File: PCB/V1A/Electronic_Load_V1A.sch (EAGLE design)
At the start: 139 parts, among them IC201 OPA77P, IC202 OPA77P, IC203 OPA77P, IC204 OPA77P, IC205 OPA77P, IC301 MAX743CPE, IC302 7805T, IC303 7805T, IC304 7905, J101 +, J102 -, J103 +, J104 -, Q101 SIRC10DP, Q102 SIRC10DP, Q103 SIRC10DP, Q104 IXTK102N65X2PADUP-, Q105 SIRC10DP, Q106 SIRC10DP, Q107 SIRC10DP, Q108 IXTK102N65X2PADUP, U201 LTC1865-MSOP, U202 LTC1865-MSOP, U203 LTC1865-MSOP, U401 AD420, U402 AD420, U403 LT1014

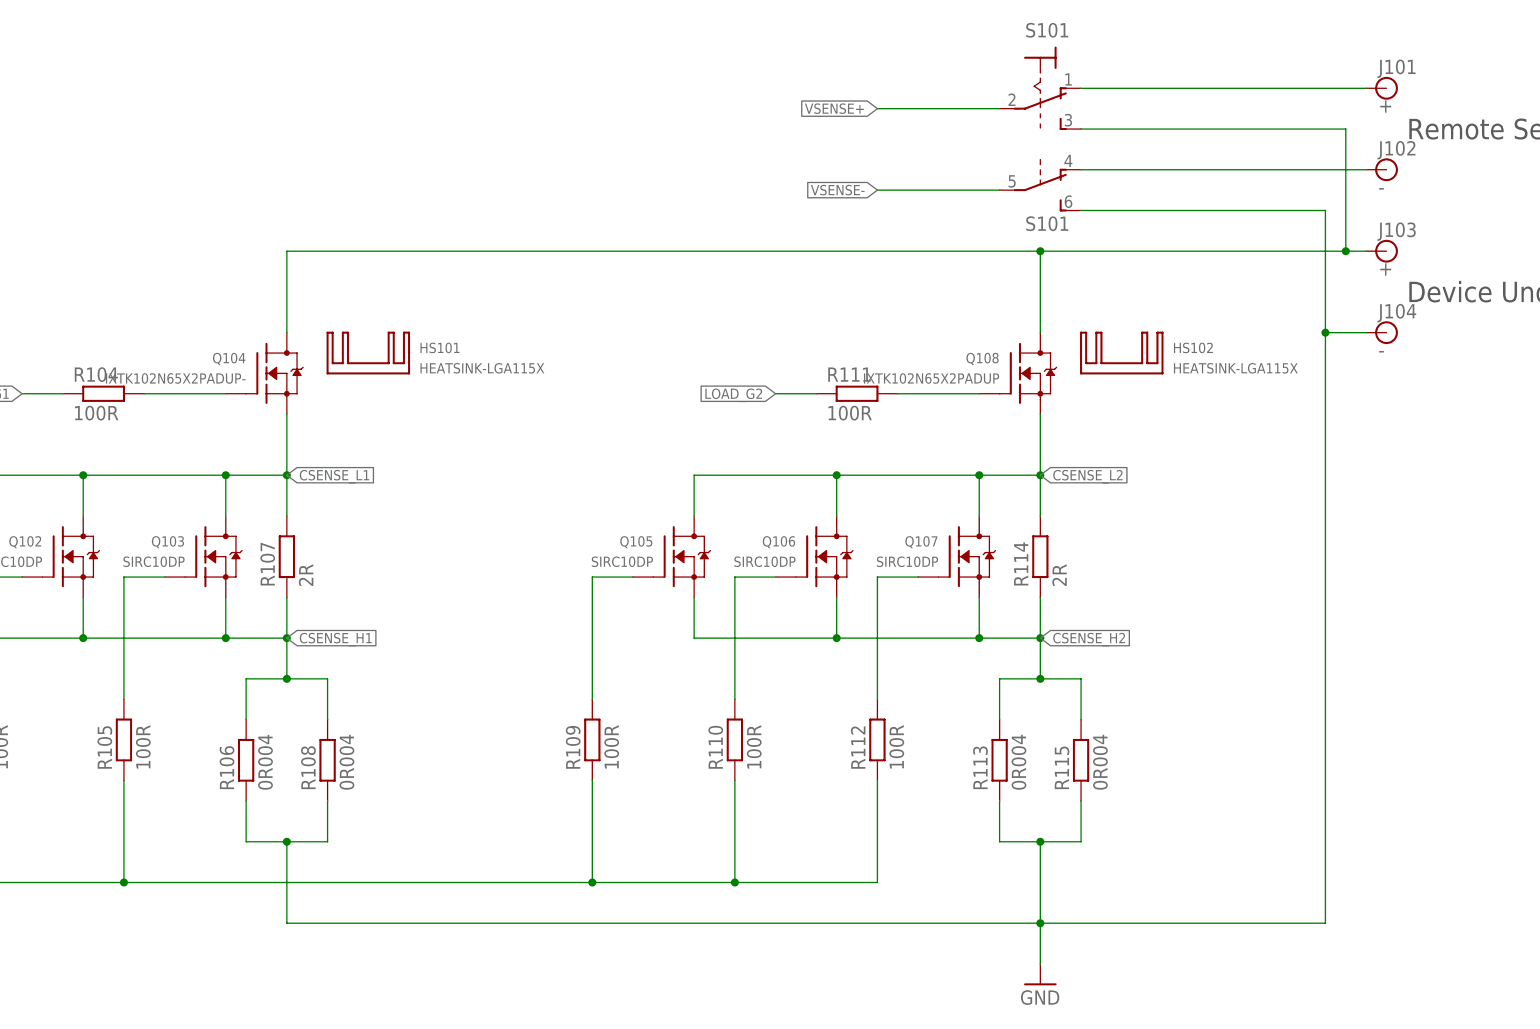
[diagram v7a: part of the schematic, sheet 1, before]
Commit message: Board layout work
PCB is 100x100mm 2 layer 2oz. MOSFETs mounted between a plate and heatsinks, control board mounted under the plate. DUT+ connected directly from binding post to drains, gates and sources connected to PCB with wires.
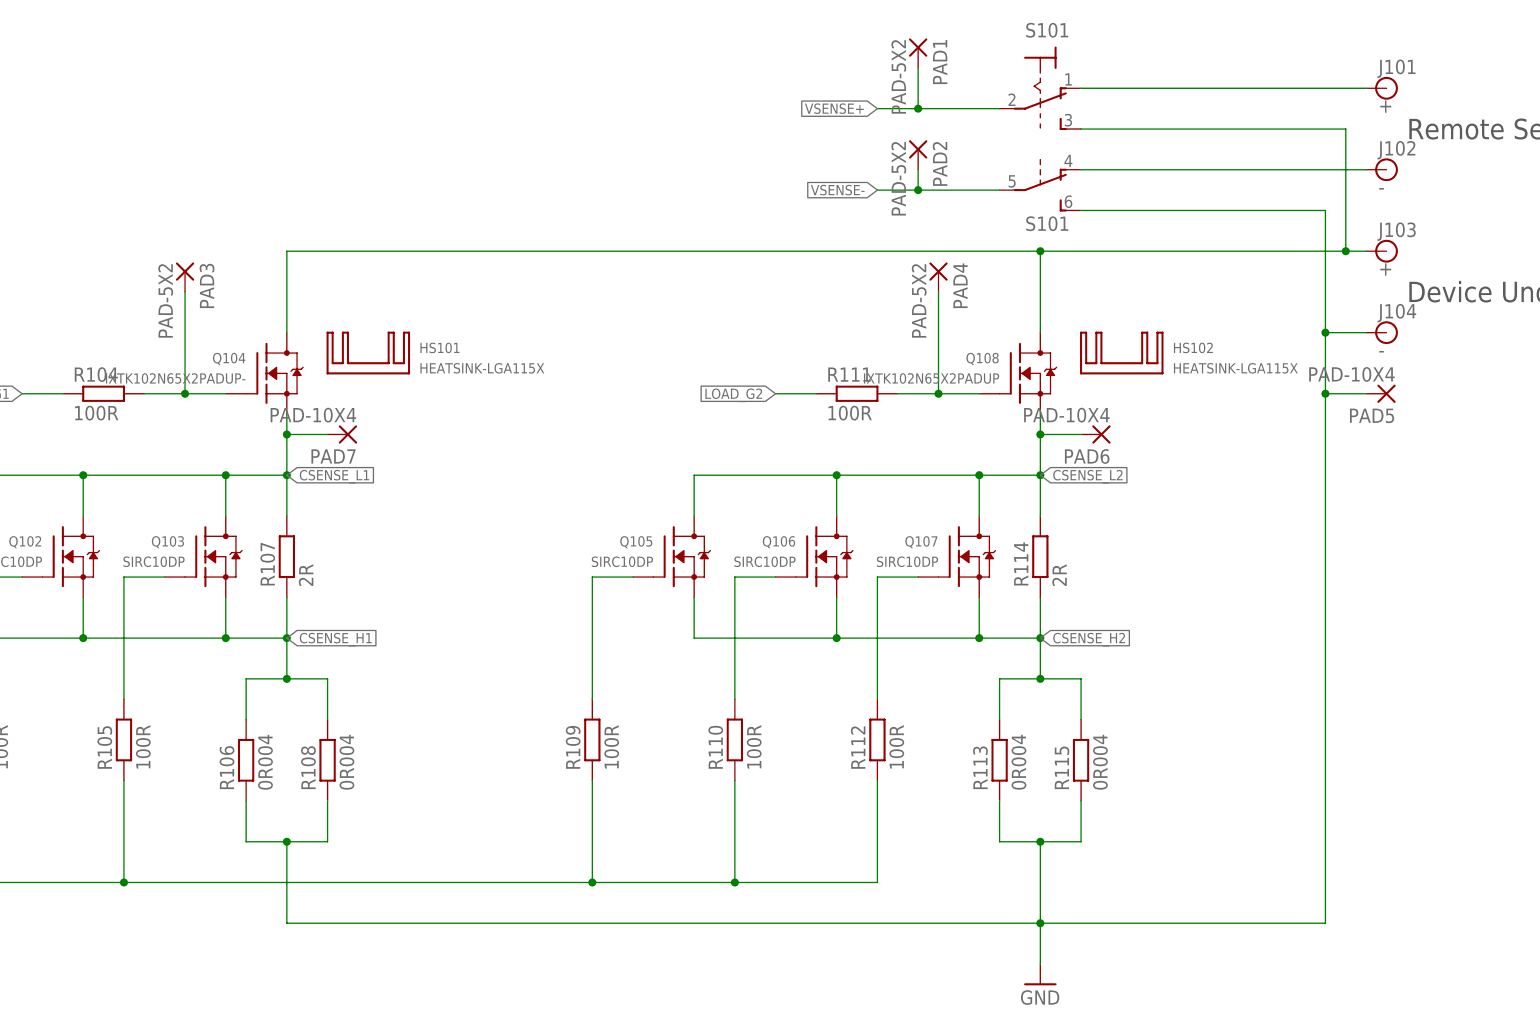
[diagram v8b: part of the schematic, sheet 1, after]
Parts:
- added PAD1, PAD2, PAD3, PAD4: PAD-5X2, pads:PAD-5X2
- added PAD5, PAD6, PAD7: PAD-10X4, pads:PAD-10X4
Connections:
- net CSENSE_L1: now also PAD7.P
- net CSENSE_L2: now also PAD6.P
- net GND: now also PAD5.P
- net N$52: now also PAD3.P
- net N$54: now also PAD4.P
- net VSENSE+: now also PAD1.P
- net VSENSE-: now also PAD2.P
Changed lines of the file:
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@@
 <?xml version="1.0" encoding="utf-8"?>
 <!DOCTYPE eagle SYSTEM "eagle.dtd">
-<eagle version="9.0.1">
+<eagle version="9.0.0">
 <drawing>
 <settings>
@@
 </variantdefs>
 <classes>
-<class number="0" name="default" width="0.2032" drill="0">
+<class number="0" name="default" width="0.1524" drill="0">
 <clearance class="0" value="0.2032"/>
 </class>
-<class number="1" name="HV" width="0.2032" drill="0">
-<clearance class="1" value="3.85"/>
+<class number="1" name="500V" width="0.1524" drill="0">
+<clearance class="1" value="3.5"/>
+</class>
+<class number="2" name="50V" width="0" drill="0">
+<clearance class="2" value="0.6"/>
 </class>
 </classes>
@@
 <part name="GND212" library="supply1" library_urn="urn:adsk.eagle:library:371" deviceset="GND" device=""/>
 <part name="P-205" library="supply1" library_urn="urn:adsk.eagle:library:371" deviceset="-15V" device=""/>
+<part name="PAD3" library="pads" deviceset="PAD" device="-5X2"/>
+<part name="PAD4" library="pads" deviceset="PAD" device="-5X2"/>
+<part name="PAD1" library="pads" deviceset="PAD" device="-5X2"/>
+<part name="PAD2" library="pads" deviceset="PAD" device="-5X2"/>
+<part name="PAD5" library="pads" deviceset="PAD" device="-10X4"/>
+<part name="PAD6" library="pads" deviceset="PAD" device="-10X4"/>
+<part name="PAD7" library="pads" deviceset="PAD" device="-10X4"/>
 </parts>
 <sheets>
@@
 <instance part="R108" gate="G$1" x="99.06" y="86.36" rot="R90"/>
 <instance part="R115" gate="G$1" x="193.04" y="86.36" rot="R90"/>
+<instance part="PAD3" gate="G$1" x="81.28" y="147.32" rot="R270"/>
+<instance part="PAD4" gate="G$1" x="175.26" y="147.32" rot="R270"/>
+<instance part="PAD1" gate="G$1" x="172.72" y="175.26" rot="R270"/>
+<instance part="PAD2" gate="G$1" x="172.72" y="162.56" rot="R270"/>
+<instance part="PAD5" gate="G$1" x="231.14" y="132.08" rot="R180"/>
+<instance part="PAD6" gate="G$1" x="195.58" y="127" rot="R180"/>
+<instance part="PAD7" gate="G$1" x="101.6" y="127" rot="R180"/>
 </instances>
 <busses>
@@
 <wire x1="223.52" y1="154.94" x2="223.52" y2="139.7" width="0.1524" layer="91"/>
 <junction x="223.52" y="139.7"/>
-<wire x1="223.52" y1="139.7" x2="223.52" y2="66.04" width="0.1524" layer="91"/>
+<wire x1="223.52" y1="139.7" x2="223.52" y2="132.08" width="0.1524" layer="91"/>
+<wire x1="223.52" y1="132.08" x2="223.52" y2="66.04" width="0.1524" layer="91"/>
 <wire x1="223.52" y1="66.04" x2="187.96" y2="66.04" width="0.1524" layer="91"/>
 <pinref part="R108" gate="G$1" pin="1"/>
@@
 <wire x1="187.96" y1="76.2" x2="187.96" y2="66.04" width="0.1524" layer="91"/>
 <junction x="187.96" y="76.2"/>
+<pinref part="PAD5" gate="G$1" pin="P"/>
+<wire x1="228.6" y1="132.08" x2="223.52" y2="132.08" width="0.1524" layer="91"/>
+<junction x="223.52" y="132.08"/>
 </segment>
 </net>
 <net name="N$52" class="0">
 <segment>
-<wire x1="76.2" y1="132.08" x2="86.36" y2="132.08" width="0.1524" layer="91"/>
+<wire x1="76.2" y1="132.08" x2="81.28" y2="132.08" width="0.1524" layer="91"/>
 <pinref part="R104" gate="G$1" pin="2"/>
 <pinref part="Q104" gate="G$1" pin="G"/>
+<pinref part="PAD3" gate="G$1" pin="P"/>
+<wire x1="81.28" y1="132.08" x2="86.36" y2="132.08" width="0.1524" layer="91"/>
+<wire x1="81.28" y1="144.78" x2="81.28" y2="132.08" width="0.1524" layer="91"/>
+<junction x="81.28" y="132.08"/>
 </segment>
 </net>
@@
 <segment>
 <pinref part="S101" gate="B" pin="P"/>
-<wire x1="182.88" y1="157.48" x2="167.64" y2="157.48" width="0.1524" layer="91"/>
+<wire x1="182.88" y1="157.48" x2="172.72" y2="157.48" width="0.1524" layer="91"/>
 <label x="167.64" y="157.48" size="1.27" layer="95" font="vector" ratio="12" rot="R180" xref="yes"/>
-</segment>
-</net>
-<net name="VSENSE+" class="0">
+<wire x1="172.72" y1="157.48" x2="167.64" y2="157.48" width="0.1524" layer="91"/>
+<wire x1="172.72" y1="160.02" x2="172.72" y2="157.48" width="0.1524" layer="91"/>
+<junction x="172.72" y="157.48"/>
+<pinref part="PAD2" gate="G$1" pin="P"/>
+</segment>
+</net>
+<net name="VSENSE+" class="1">
 <segment>
 <pinref part="S101" gate="1" pin="P"/>
-<wire x1="182.88" y1="167.64" x2="167.64" y2="167.64" width="0.1524" layer="91"/>
+<wire x1="182.88" y1="167.64" x2="172.72" y2="167.64" width="0.1524" layer="91"/>
 <label x="167.64" y="167.64" size="1.27" layer="95" font="vector" ratio="12" rot="R180" xref="yes"/>
+<wire x1="172.72" y1="167.64" x2="167.64" y2="167.64" width="0.1524" layer="91"/>
+<wire x1="172.72" y1="172.72" x2="172.72" y2="167.64" width="0.1524" layer="91"/>
+<junction x="172.72" y="167.64"/>
+<pinref part="PAD1" gate="G$1" pin="P"/>
 </segment>
 </net>
@@
 <segment>
 <pinref part="R111" gate="G$1" pin="2"/>
-<wire x1="170.18" y1="132.08" x2="180.34" y2="132.08" width="0.1524" layer="91"/>
+<wire x1="170.18" y1="132.08" x2="175.26" y2="132.08" width="0.1524" layer="91"/>
 <pinref part="Q108" gate="G$1" pin="G"/>
+<pinref part="PAD4" gate="G$1" pin="P"/>
+<wire x1="175.26" y1="132.08" x2="180.34" y2="132.08" width="0.1524" layer="91"/>
+<wire x1="175.26" y1="144.78" x2="175.26" y2="132.08" width="0.1524" layer="91"/>
+<junction x="175.26" y="132.08"/>
 </segment>
 </net>
@@
 <label x="93.98" y="121.92" size="1.27" layer="95" font="vector" ratio="12" xref="yes"/>
 <pinref part="Q104" gate="G$1" pin="S"/>
-<wire x1="93.98" y1="129.54" x2="93.98" y2="121.92" width="0.1524" layer="91"/>
+<wire x1="93.98" y1="129.54" x2="93.98" y2="127" width="0.1524" layer="91"/>
 <junction x="93.98" y="121.92"/>
 <pinref part="Q102" gate="G$1" pin="D"/>
+<wire x1="93.98" y1="127" x2="93.98" y2="121.92" width="0.1524" layer="91"/>
 <wire x1="68.58" y1="116.84" x2="68.58" y2="121.92" width="0.1524" layer="91"/>
 <pinref part="Q101" gate="G$1" pin="D"/>
@@
 <wire x1="86.36" y1="116.84" x2="86.36" y2="121.92" width="0.1524" layer="91"/>
 <junction x="86.36" y="121.92"/>
+<pinref part="PAD7" gate="G$1" pin="P"/>
+<wire x1="99.06" y1="127" x2="93.98" y2="127" width="0.1524" layer="91"/>
+<junction x="93.98" y="127"/>
 </segment>
 </net>
@@
 <label x="187.96" y="121.92" size="1.27" layer="95" font="vector" ratio="12" xref="yes"/>
 <pinref part="Q108" gate="G$1" pin="S"/>
-<wire x1="187.96" y1="129.54" x2="187.96" y2="121.92" width="0.1524" layer="91"/>
+<wire x1="187.96" y1="129.54" x2="187.96" y2="127" width="0.1524" layer="91"/>
 <junction x="187.96" y="121.92"/>
 <pinref part="Q107" gate="G$1" pin="D"/>
+<wire x1="187.96" y1="127" x2="187.96" y2="121.92" width="0.1524" layer="91"/>
 <wire x1="180.34" y1="116.84" x2="180.34" y2="121.92" width="0.1524" layer="91"/>
 <junction x="180.34" y="121.92"/>
@@
 <wire x1="144.78" y1="121.92" x2="162.56" y2="121.92" width="0.1524" layer="91"/>
 <junction x="162.56" y="121.92"/>
+<pinref part="PAD6" gate="G$1" pin="P"/>
+<wire x1="193.04" y1="127" x2="187.96" y2="127" width="0.1524" layer="91"/>
+<junction x="187.96" y="127"/>
 </segment>
 </net>
@@
 </segment>
 </net>
-<net name="N$73" class="0">
+<net name="N$73" class="2">
 <segment>
 <pinref part="R216" gate="G$1" pin="2"/>
@@
 </segment>
 </net>
-<net name="N$78" class="0">
+<net name="N$78" class="2">
 <segment>
 <pinref part="R211" gate="G$1" pin="1"/>
@@
 </segment>
 </net>
-<net name="N$79" class="0">
+<net name="N$79" class="2">
 <segment>
 <pinref part="R212" gate="G$1" pin="1"/>
@@
 </segment>
 </net>
-<net name="N$84" class="0">
+<net name="N$84" class="2">
 <segment>
 <pinref part="R213" gate="G$1" pin="1"/>
@@
 </segment>
 </net>
-<net name="N$85" class="0">
+<net name="N$85" class="2">
 <segment>
 <pinref part="R210" gate="G$1" pin="2"/>
@@
 </segment>
 </net>
-<net name="N$86" class="0">
+<net name="N$86" class="2">
 <segment>
 <pinref part="R209" gate="G$1" pin="2"/>
@@
 </segment>
 </net>
-<net name="N$87" class="0">
+<net name="N$87" class="2">
 <segment>
 <pinref part="R208" gate="G$1" pin="2"/>
@@
 </segment>
 </net>
-<net name="N$88" class="0">
+<net name="N$88" class="2">
 <segment>
 <pinref part="R201" gate="G$1" pin="1"/>
@@
 </segment>
 </net>
-<net name="N$89" class="0">
+<net name="N$89" class="2">
 <segment>
 <pinref part="R202" gate="G$1" pin="1"/>
@@
 </segment>
 </net>
-<net name="VSENSE+" class="0">
+<net name="VSENSE+" class="1">
 <segment>
 <pinref part="R203" gate="G$1" pin="1"/>
